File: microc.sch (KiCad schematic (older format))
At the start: 17 parts, among them J1 Conn_01x12, J2 Conn_01x12, J3 USB_C_Receptacle_USB2.0, U1 ATmega32U4-AU, U2 USBLC6-2SC6

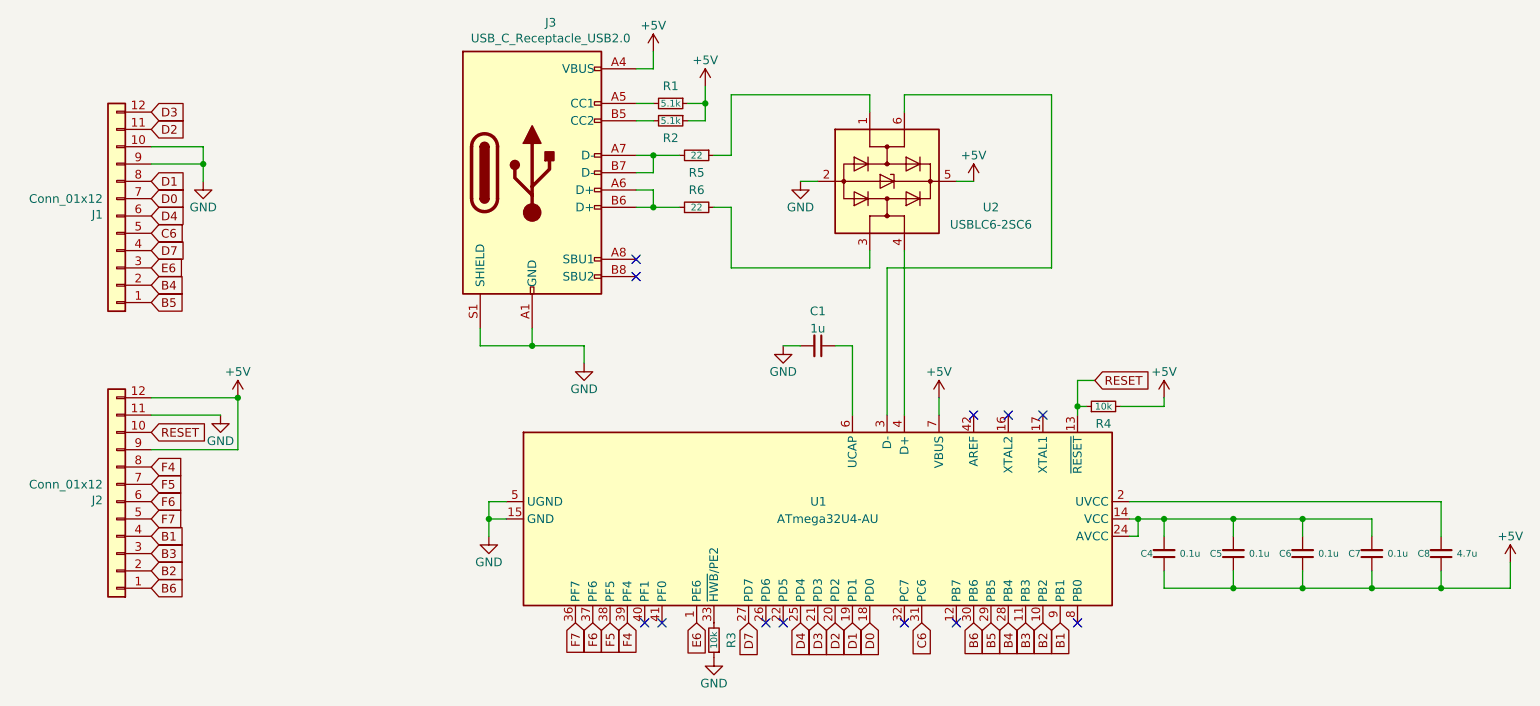
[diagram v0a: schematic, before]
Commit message: rev 1 - Completed PCB - Completed schematic
Notes:
- Added 0 ohm resistor to schematic in order to help with routing
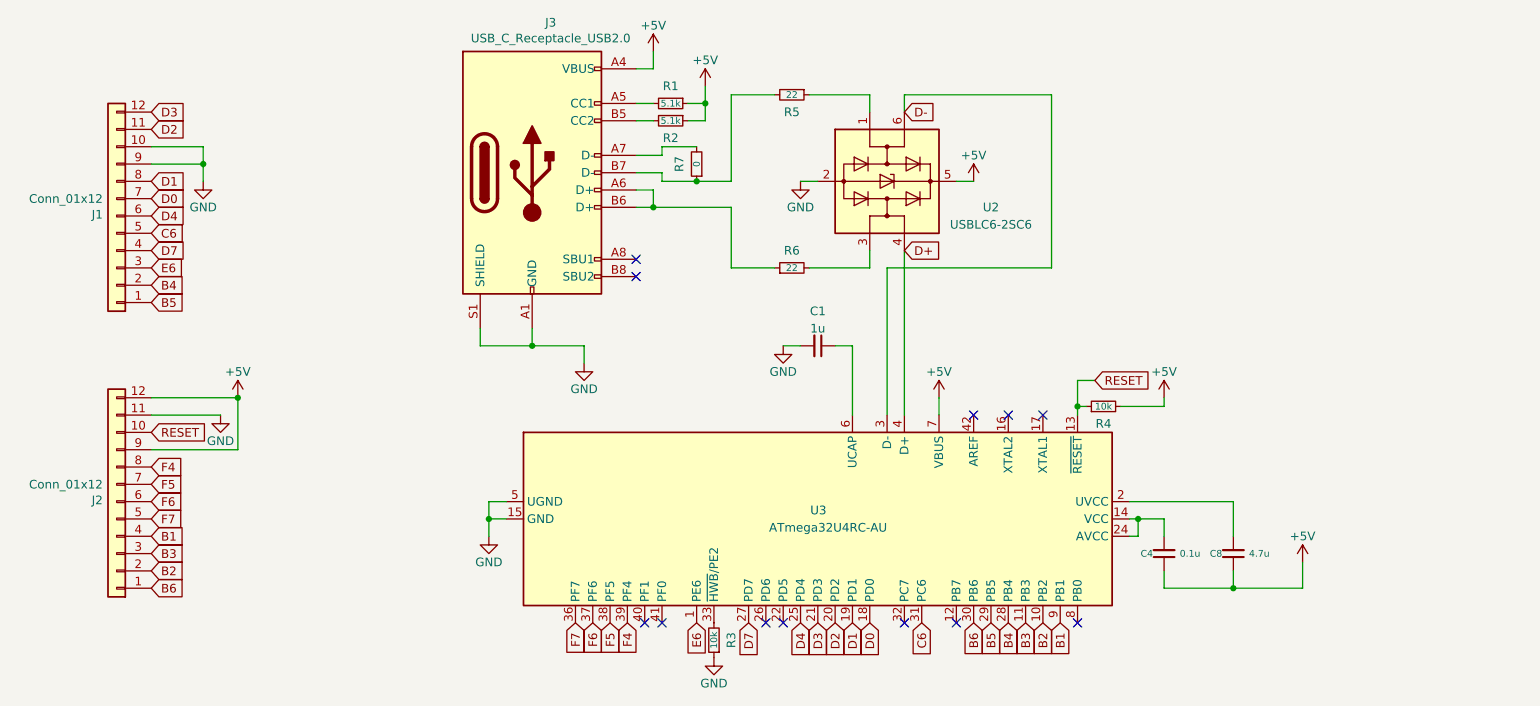
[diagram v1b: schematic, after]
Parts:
- removed C5, C6, C7: 0.1u, Capacitor_SMD:C_0603_1608Metric, symbol Device:C_Small
- removed U1: ATmega32U4-AU, Package_QFP:TQFP-44_10x10mm_P0.8mm, symbol MCU_Microchip_ATmega:ATmega32U4-AU
- added R7: 0, Resistor_SMD:R_0603_1608Metric, symbol Device:R_Small
- added U3: ATmega32U4RC-AU, Package_QFP:TQFP-44_10x10mm_P0.8mm, symbol MCU_Microchip_ATmega:ATmega32U4RC-AU
- J3: footprint Connector_USB:USB_C_Receptacle_HRO_TYPE-C-31-M-12 -> kiboard:USB-C_16P_Midmount
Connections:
- net +5V: now also U3.7 (VBUS)
- net B1: now also U3.9 (PB1)
- net B2: now also U3.10 (PB2)
- net B3: now also U3.11 (PB3)
- net B4: now also U3.28 (PB4)
- net B5: now also U3.29 (PB5)
- net B6: now also U3.30 (PB6)
- net C6: now also U3.31 (PC6)
- net D0: now also U3.18 (PD0)
- net D1: now also U3.19 (PD1)
- net D2: now also U3.20 (PD2)
- net D3: now also U3.21 (PD3)
- net D4: now also U3.25 (PD4)
- net D7: now also U3.27 (PD7)
- net E6: now also U3.1 (PE6)
- net F4: now also U3.39 (PF4)
- net F5: now also U3.38 (PF5)
- net F6: now also U3.37 (PF6)
- net F7: now also U3.36 (PF7)
- net GND: now also U3.15 (GND), U3.23 (GND), U3.35 (GND), U3.43 (GND), U3.5 (UGND)
- net RESET: now also U3.13 (~RESET)
- net at C4.2: now also U3.14 (VCC), U3.24 (AVCC), U3.34 (VCC), U3.44 (AVCC)
- net at C8.2: now also U3.2 (UVCC)
- net D-: now reaches U2.6 (I/O1)
- net D-: now also U3.3 (D-)
- net at R3.2: now also U3.33 (~HWB~/PE2)
- net D+: now reaches U2.4 (I/O2)
- net D+: now also U3.4 (D+)
- net at C1.1: now also U3.6 (UCAP)
- net at J3.B7 (D-), R5.2: now also R7.1; no longer J3.A7 (D-)
- new net: J3.A7 (D-), R7.2
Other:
- moved on the sheet: C8, R5, R6
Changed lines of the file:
@@
 $EndDescr
-$Comp
-L MCU_Microchip_ATmega:ATmega32U4-AU U1
-U 1 1 60FE5969
-P 6400 4700
-F 0 "U1" V 6300 4750 50  0000 R CNN
-F 1 "ATmega32U4-AU" V 6400 5050 50  0000 R CNN
-F 2 "Package_QFP:TQFP-44_10x10mm_P0.8mm" H 6400 4700 50  0001 C CIN
-F 3 "http://ww1.microchip.com/downloads/en/DeviceDoc/Atmel-7766-8-bit-AVR-ATmega16U4-32U4_Datasheet.pdf" H 6400 4700 50  0001 C CNN
-	1    6400 4700
-	0    1    1    0
-$EndComp
 $Comp
 L Connector:USB_C_Receptacle_USB2.0 J3
@@
 F 0 "J3" H 4857 3567 50  0000 C CNN
 F 1 "USB_C_Receptacle_USB2.0" H 4857 3476 50  0000 C CNN
-F 2 "Connector_USB:USB_C_Receptacle_HRO_TYPE-C-31-M-12" H 4900 2700 50  0001 C CNN
+F 2 "kiboard:USB-C_16P_Midmount" H 4900 2700 50  0001 C CNN
 F 3 "https://www.usb.org/sites/default/files/documents/usb_type-c.zip" H 4900 2700 50  0001 C CNN
 	1    4750 2700
@@
 	5750 2300 5750 2200
 Wire Wire Line
-	5350 2700 5450 2700
-Wire Wire Line
-	5450 2700 5450 2600
-Wire Wire Line
-	5450 2600 5350 2600
-Wire Wire Line
-	5450 2600 5600 2600
-Wire Wire Line
-	5900 2600 5900 2250
-Connection ~ 5450 2600
-Wire Wire Line
 	5350 2800 5450 2800
 Wire Wire Line
@@
 	6700 2250 6700 2350
 Wire Wire Line
-	5900 2250 6700 2250
-Wire Wire Line
-	5450 2900 5600 2900
+	5900 2250 6150 2250
 Wire Wire Line
 	5900 2900 5900 3250
@@
 	6700 3250 6700 3150
 Wire Wire Line
-	5900 3250 6700 3250
+	5900 3250 6150 3250
 Wire Wire Line
 	6900 2350 6900 2250
@@
 Wire Wire Line
 	4500 4700 4500 4600
-Connection ~ 9200 4700
-Wire Wire Line
-	9200 4700 9600 4700
-Connection ~ 8800 4700
-Wire Wire Line
-	8800 4700 9200 4700
 Wire Wire Line
 	8400 4800 8400 4700
-Connection ~ 8400 4700
-Wire Wire Line
-	8400 4700 8800 4700
-Wire Wire Line
-	10000 4600 10000 4800
-Wire Wire Line
-	9600 4700 9600 4800
-Wire Wire Line
-	9200 4800 9200 4700
-Wire Wire Line
-	8800 4800 8800 4700
-Wire Wire Line
-	8800 5100 9200 5100
 Connection ~ 8800 5100
 Wire Wire Line
 	8800 5000 8800 5100
-Wire Wire Line
-	9200 5100 9600 5100
-Connection ~ 9200 5100
-Wire Wire Line
-	9200 5000 9200 5100
-Wire Wire Line
-	9600 5100 10000 5100
-Connection ~ 9600 5100
-Wire Wire Line
-	9600 5000 9600 5100
-Wire Wire Line
-	10000 5100 10000 5000
 Wire Wire Line
 	8400 5100 8800 5100
@@
 L Device:C_Small C8
 U 1 1 6118D688
-P 10000 4900
-F 0 "C8" H 10100 4900 39  0000 C CNN
-F 1 "4.7u" H 9850 4900 39  0000 C CNN
-F 2 "Capacitor_SMD:C_0603_1608Metric" H 10000 4900 50  0001 C CNN
-F 3 "~" H 10000 4900 50  0001 C CNN
-	1    10000 4900
-	-1   0    0    1
-$EndComp
-$Comp
-L Device:C_Small C7
-U 1 1 6118D2F6
-P 9600 4900
-F 0 "C7" H 9700 4900 39  0000 C CNN
-F 1 "0.1u" H 9450 4900 39  0000 C CNN
-F 2 "Capacitor_SMD:C_0603_1608Metric" H 9600 4900 50  0001 C CNN
-F 3 "~" H 9600 4900 50  0001 C CNN
-	1    9600 4900
-	-1   0    0    1
-$EndComp
-$Comp
-L Device:C_Small C6
-U 1 1 6118CF48
-P 9200 4900
-F 0 "C6" H 9300 4900 39  0000 C CNN
-F 1 "0.1u" H 9050 4900 39  0000 C CNN
-F 2 "Capacitor_SMD:C_0603_1608Metric" H 9200 4900 50  0001 C CNN
-F 3 "~" H 9200 4900 50  0001 C CNN
-	1    9200 4900
-	-1   0    0    1
-$EndComp
-$Comp
-L Device:C_Small C5
-U 1 1 6118C778
 P 8800 4900
-F 0 "C5" H 8900 4900 39  0000 C CNN
-F 1 "0.1u" H 8650 4900 39  0000 C CNN
+F 0 "C8" H 8900 4900 39  0000 C CNN
+F 1 "4.7u" H 8650 4900 39  0000 C CNN
 F 2 "Capacitor_SMD:C_0603_1608Metric" H 8800 4900 50  0001 C CNN
 F 3 "~" H 8800 4900 50  0001 C CNN
@@
 Connection ~ 8250 4700
 Wire Wire Line
-	8200 4600 10000 4600
+	8200 4600 8800 4600
 Connection ~ 4750 3700
 $Comp
@@
 NoConn ~ 7700 4100
 NoConn ~ 7500 4100
-Wire Wire Line
-	5800 2600 5900 2600
 $Comp
 L Device:R_Small R5
 U 1 1 61406714
-P 5700 2600
-F 0 "R5" V 5800 2600 50  0000 C CNN
-F 1 "22" V 5700 2600 39  0000 C CNN
-F 2 "Resistor_SMD:R_0603_1608Metric" H 5700 2600 50  0001 C CNN
-F 3 "~" H 5700 2600 50  0001 C CNN
-	1    5700 2600
+P 6250 2250
+F 0 "R5" V 6350 2250 50  0000 C CNN
+F 1 "22" V 6250 2250 39  0000 C CNN
+F 2 "Resistor_SMD:R_0603_1608Metric" H 6250 2250 50  0001 C CNN
+F 3 "~" H 6250 2250 50  0001 C CNN
+	1    6250 2250
 	0    1    1    0
 $EndComp
@@
 L Device:R_Small R6
 U 1 1 61409009
-P 5700 2900
-F 0 "R6" V 5800 2900 50  0000 C CNN
-F 1 "22" V 5700 2900 39  0000 C CNN
-F 2 "Resistor_SMD:R_0603_1608Metric" H 5700 2900 50  0001 C CNN
-F 3 "~" H 5700 2900 50  0001 C CNN
-	1    5700 2900
+P 6250 3250
+F 0 "R6" V 6350 3250 50  0000 C CNN
+F 1 "22" V 6250 3250 39  0000 C CNN
+F 2 "Resistor_SMD:R_0603_1608Metric" H 6250 3250 50  0001 C CNN
+F 3 "~" H 6250 3250 50  0001 C CNN
+	1    6250 3250
 	0    -1   -1   0
 $EndComp
-Wire Wire Line
-	5800 2900 5900 2900
 $Comp
 L power:+5V #PWR0106
 U 1 1 6142AA7E
-P 10400 4950
-F 0 "#PWR0106" H 10400 4800 50  0001 C CNN
-F 1 "+5V" H 10400 5100 50  0000 C CNN
-F 2 "" H 10400 4950 50  0001 C CNN
-F 3 "" H 10400 4950 50  0001 C CNN
-	1    10400 4950
-	1    0    0    -1
-$EndComp
-Wire Wire Line
-	10000 5100 10400 5100
-Wire Wire Line
-	10400 5100 10400 4950
-Connection ~ 10000 5100
+P 9200 4950
+F 0 "#PWR0106" H 9200 4800 50  0001 C CNN
+F 1 "+5V" H 9200 5100 50  0000 C CNN
+F 2 "" H 9200 4950 50  0001 C CNN
+F 3 "" H 9200 4950 50  0001 C CNN
+	1    9200 4950
+	1    0    0    -1
+$EndComp
+Wire Wire Line
+	9200 5100 9200 4950
+Wire Wire Line
+	8800 5100 9200 5100
+Wire Wire Line
+	8800 4800 8800 4600
+$Comp
+L MCU_Microchip_ATmega:ATmega32U4RC-AU U3
+U 1 1 60FFCB9D
+P 6400 4700
+F 0 "U3" V 6350 4750 50  0000 R CNN
+F 1 "ATmega32U4RC-AU" V 6450 5100 50  0000 R CNN
+F 2 "Package_QFP:TQFP-44_10x10mm_P0.8mm" H 6400 4700 50  0001 C CIN
+F 3 "http://ww1.microchip.com/downloads/en/DeviceDoc/Atmel-7766-8-bit-AVR-ATmega16U4-32U4_Datasheet.pdf" H 6400 4700 50  0001 C CNN
+	1    6400 4700
+	0    1    1    0
+$EndComp
+Text GLabel 6900 3150 2    50   Input ~ 0
+D+
+Text GLabel 6900 2350 2    50   Input ~ 0
+D-
+$Comp
+L Device:R_Small R7
+U 1 1 6102E257
+P 5700 2650
+F 0 "R7" V 5800 2650 50  0000 C CNN
+F 1 "0" V 5700 2650 39  0000 C CNN
+F 2 "Resistor_SMD:R_0603_1608Metric" H 5700 2650 50  0001 C CNN
+F 3 "~" H 5700 2650 50  0001 C CNN
+	1    5700 2650
+	-1   0    0    1
+$EndComp
+Wire Wire Line
+	6350 2250 6700 2250
+Wire Wire Line
+	6350 3250 6700 3250
+Wire Wire Line
+	5450 2900 5900 2900
+Wire Wire Line
+	5700 2750 5500 2750
+Wire Wire Line
+	5500 2750 5500 2700
+Wire Wire Line
+	5500 2700 5350 2700
+Wire Wire Line
+	5350 2600 5500 2600
+Wire Wire Line
+	5500 2600 5500 2550
+Wire Wire Line
+	5500 2550 5700 2550
+Wire Wire Line
+	5700 2750 5900 2750
+Connection ~ 5700 2750
+Wire Wire Line
+	5900 2250 5900 2750
 $EndSCHEMATC

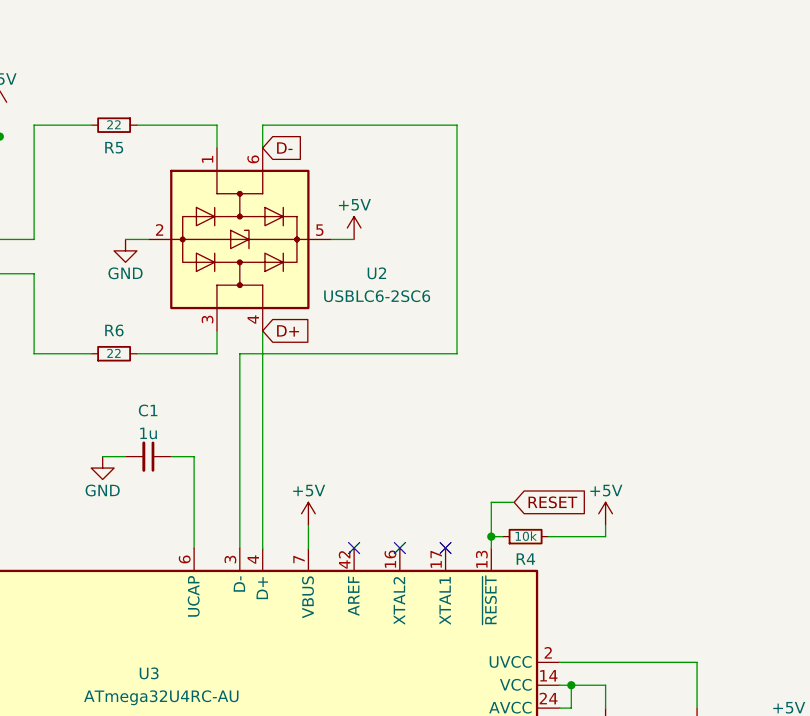
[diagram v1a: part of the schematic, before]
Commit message: rev1.1 - Added crystal to PCB
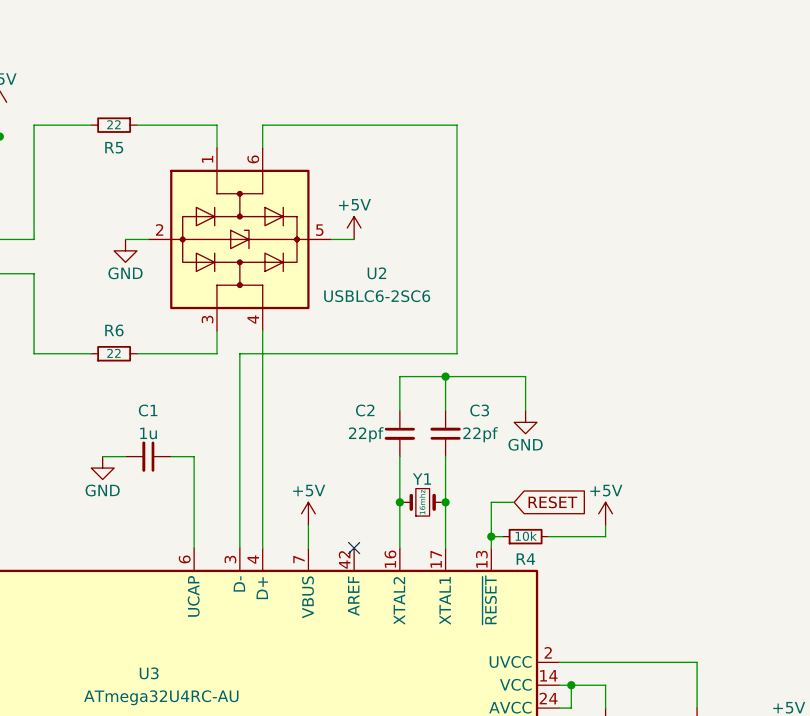
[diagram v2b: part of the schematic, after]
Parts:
- added C2, C3: 22pf, Capacitor_SMD:C_0603_1608Metric, symbol Device:C_Small
- added Y1: 16mhz, Crystal:Crystal_SMD_5032-2Pin_5.0x3.2mm_HandSoldering, symbol Device:Crystal_Small
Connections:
- net GND: now also C2.1, C3.2
- net at U3.16 (XTAL2): now also C2.2, Y1.1
- net at U3.17 (XTAL1): now also C3.1, Y1.2
- net D+: no longer names the net of U2.4 (I/O2), U3.4 (D+)
- net D-: no longer names the net of U2.6 (I/O1), U3.3 (D-)
- no-connect marks 12 -> 10
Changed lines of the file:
@@
 Wire Wire Line
 	8400 4050 8400 4000
-NoConn ~ 7700 4100
-NoConn ~ 7500 4100
 $Comp
 L Device:R_Small R5
@@
 	0    1    1    0
 $EndComp
-Text GLabel 6900 3150 2    50   Input ~ 0
-D+
-Text GLabel 6900 2350 2    50   Input ~ 0
-D-
 $Comp
 L Device:R_Small R7
@@
 Wire Wire Line
 	5900 2250 5900 2750
+$Comp
+L Device:C_Small C3
+U 1 1 610069EE
+P 7700 3600
+F 0 "C3" H 7550 3500 50  0000 C CNN
+F 1 "22pf" H 7550 3600 50  0000 C CNN
+F 2 "Capacitor_SMD:C_0603_1608Metric" H 7700 3600 50  0001 C CNN
+F 3 "~" H 7700 3600 50  0001 C CNN
+	1    7700 3600
+	-1   0    0    1
+$EndComp
+$Comp
+L Device:C_Small C2
+U 1 1 61007820
+P 7500 3600
+F 0 "C2" H 7350 3700 50  0000 C CNN
+F 1 "22pf" H 7350 3600 50  0000 C CNN
+F 2 "Capacitor_SMD:C_0603_1608Metric" H 7500 3600 50  0001 C CNN
+F 3 "~" H 7500 3600 50  0001 C CNN
+	1    7500 3600
+	1    0    0    -1
+$EndComp
+$Comp
+L Device:Crystal_Small Y1
+U 1 1 61002907
+P 7600 3900
+F 0 "Y1" H 7600 4000 50  0000 C CNN
+F 1 "16mhz" V 7600 3900 24  0000 C CNN
+F 2 "Crystal:Crystal_SMD_5032-2Pin_5.0x3.2mm_HandSoldering" H 7600 3900 50  0001 C CNN
+F 3 "~" H 7600 3900 50  0001 C CNN
+	1    7600 3900
+	1    0    0    -1
+$EndComp
+$Comp
+L power:GND #PWR0111
+U 1 1 61017ABC
+P 8050 3500
+F 0 "#PWR0111" H 8050 3250 50  0001 C CNN
+F 1 "GND" H 8050 3350 50  0000 C CNN
+F 2 "" H 8050 3500 50  0001 C CNN
+F 3 "" H 8050 3500 50  0001 C CNN
+	1    8050 3500
+	1    0    0    -1
+$EndComp
+Wire Wire Line
+	7500 3500 7500 3350
+Wire Wire Line
+	7500 3350 7700 3350
+Wire Wire Line
+	8050 3350 8050 3500
+Wire Wire Line
+	7700 3500 7700 3350
+Connection ~ 7700 3350
+Wire Wire Line
+	7700 3350 8050 3350
+Wire Wire Line
+	7700 3700 7700 3900
+Connection ~ 7700 3900
+Wire Wire Line
+	7700 3900 7700 4100
+Wire Wire Line
+	7500 4100 7500 3900
+Connection ~ 7500 3900
+Wire Wire Line
+	7500 3900 7500 3700
 $EndSCHEMATC

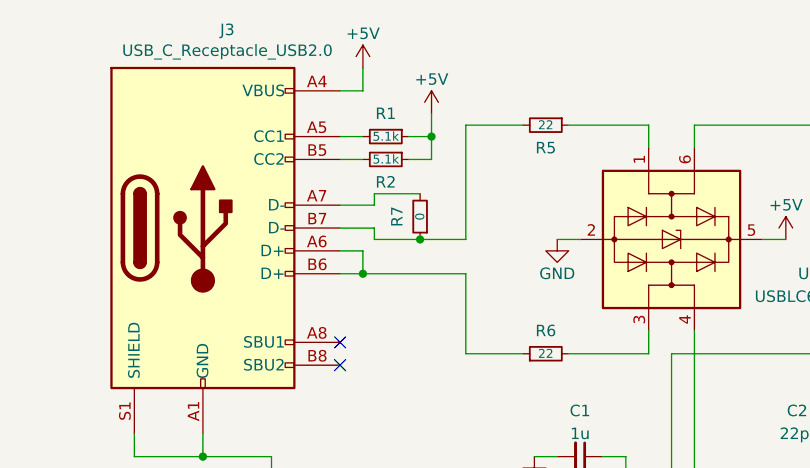
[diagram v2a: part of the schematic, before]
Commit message: rev1.2 - Removed 0 ohm resistor and replaced with via
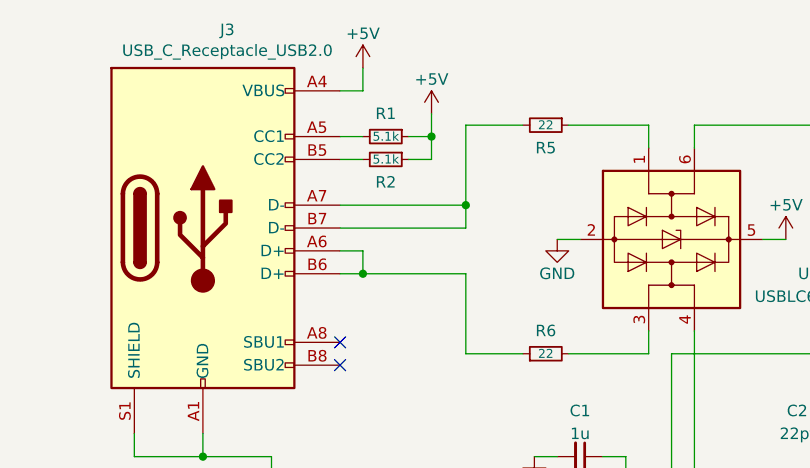
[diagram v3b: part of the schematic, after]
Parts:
- removed R7: 0, Resistor_SMD:R_0603_1608Metric, symbol Device:R_Small
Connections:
- net at J3.A7 (D-): now also J3.B7 (D-), R5.2
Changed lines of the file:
@@
 	0    1    1    0
-$EndComp
-$Comp
-L Device:R_Small R7
-U 1 1 6102E257
-P 5700 2650
-F 0 "R7" V 5800 2650 50  0000 C CNN
-F 1 "0" V 5700 2650 39  0000 C CNN
-F 2 "Resistor_SMD:R_0603_1608Metric" H 5700 2650 50  0001 C CNN
-F 3 "~" H 5700 2650 50  0001 C CNN
-	1    5700 2650
-	-1   0    0    1
 $EndComp
 Wire Wire Line
@@
 Wire Wire Line
 	5450 2900 5900 2900
-Wire Wire Line
-	5700 2750 5500 2750
-Wire Wire Line
-	5500 2750 5500 2700
-Wire Wire Line
-	5500 2700 5350 2700
-Wire Wire Line
-	5350 2600 5500 2600
-Wire Wire Line
-	5500 2600 5500 2550
-Wire Wire Line
-	5500 2550 5700 2550
-Wire Wire Line
-	5700 2750 5900 2750
-Connection ~ 5700 2750
-Wire Wire Line
-	5900 2250 5900 2750
 $Comp
 L Device:C_Small C3
@@
 Wire Wire Line
 	7500 3900 7500 3700
+Wire Wire Line
+	5900 2250 5900 2600
+Connection ~ 5900 2600
+Wire Wire Line
+	5900 2600 5900 2700
+Wire Wire Line
+	5350 2600 5900 2600
+Wire Wire Line
+	5350 2700 5900 2700
 $EndSCHEMATC
